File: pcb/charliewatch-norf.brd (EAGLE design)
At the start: 33 x 33 mm, 84 parts, among them K1 TS-1188E, U2 CC430F5137IRGZR, X1 CRYSTALS-NOGND-IQXC-25

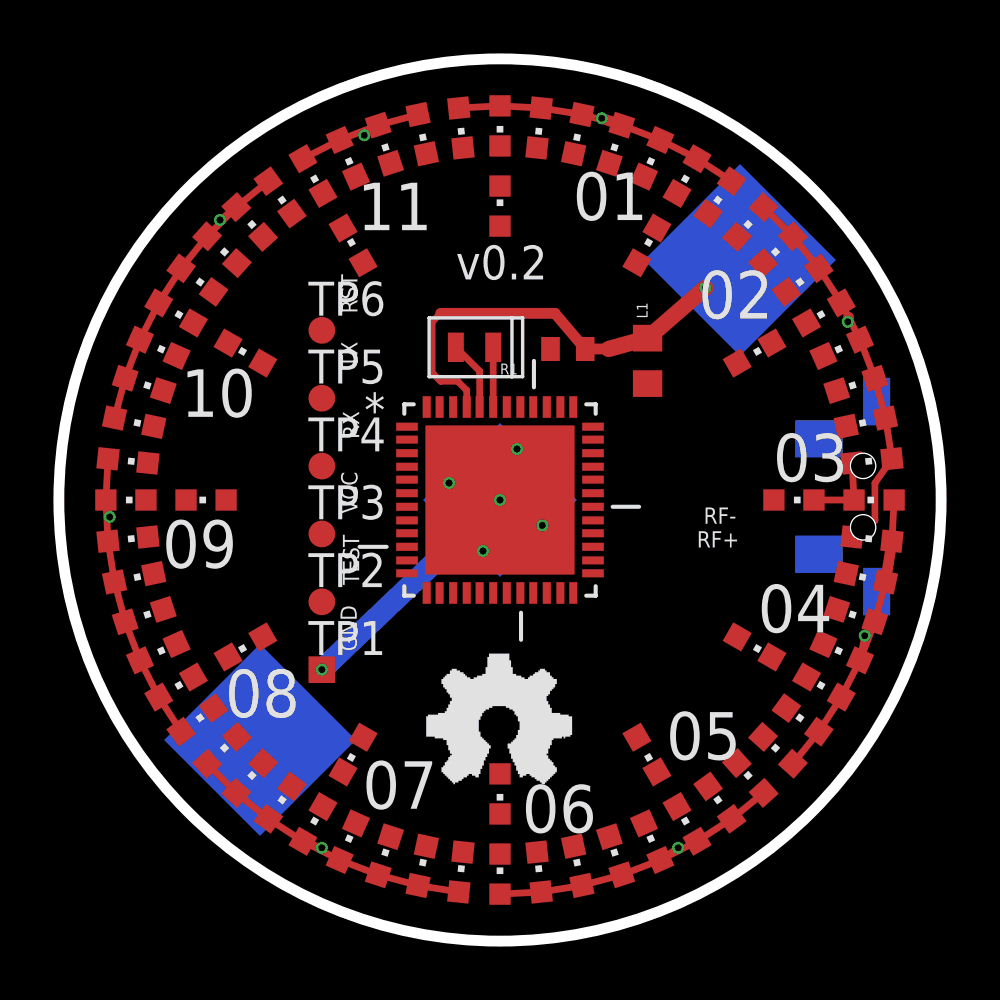
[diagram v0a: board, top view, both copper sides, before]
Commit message: slightly smaller, still routable version with no RF components
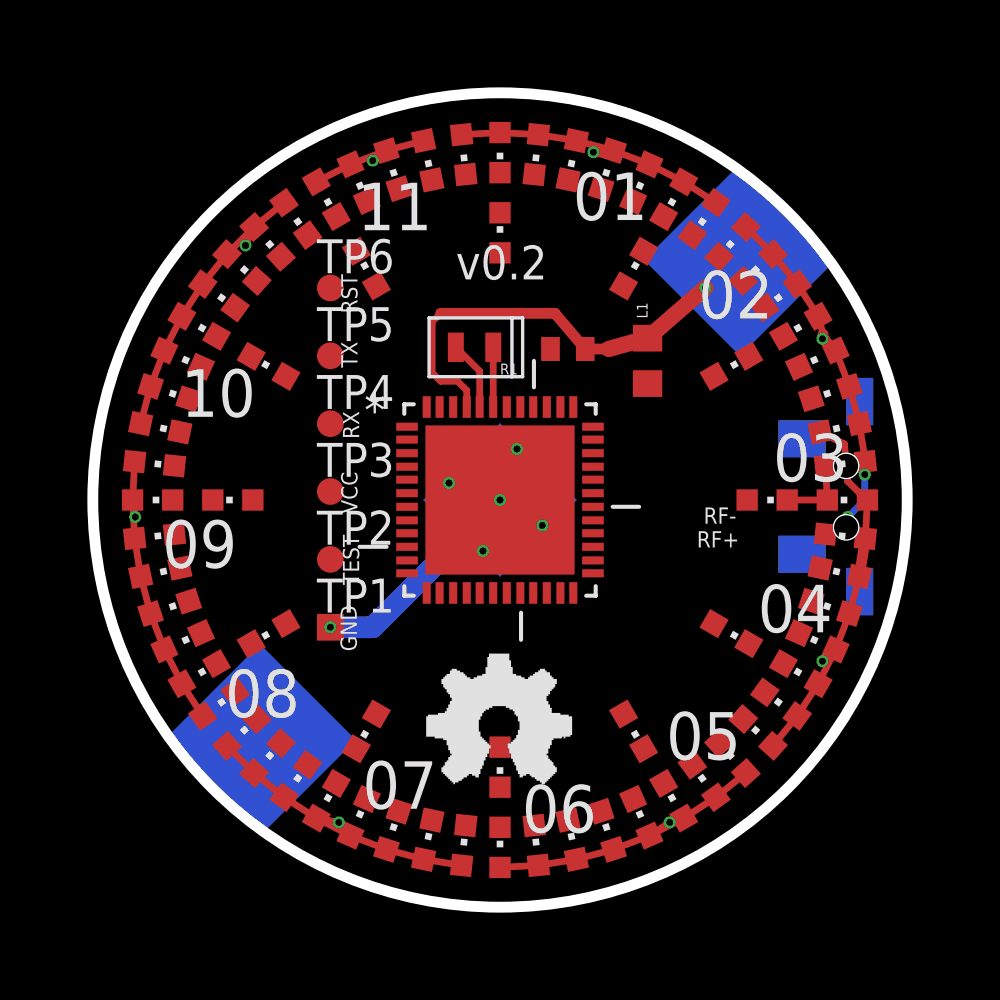
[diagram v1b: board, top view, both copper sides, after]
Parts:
- moved TP3 1.62 mm to (19.1, 25.7)
- moved TP1 1.62 mm to (19.1, 20.6)
- moved TP2 1.62 mm to (19.1, 23.2)
- moved TP4 1.62 mm to (19.1, 28.3)
- moved TP5 1.62 mm to (19.1, 30.8)
- moved TP6 1.62 mm to (19.1, 33.3)
- moved LED25 1.00 mm to (26.8, 12.5)
- moved LED32 1.00 mm to (24.0, 12.5)
- moved LED40 1.00 mm to (12.5, 26.8)
- moved LED42 1.00 mm to (12.5, 24.0)
- moved LED0 1.00 mm to (24.0, 38.3)
- moved LED17 1.00 mm to (38.3, 24.0)
- moved LED2 1.00 mm to (26.8, 38.3)
- moved LED8 1.00 mm to (38.3, 26.8)
- moved LED1 1.00 mm to (25.4, 38.4)
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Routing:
- net B2: track 11.7 -> 14.2 mm
- net GND: track 22.1 -> 21.2 mm
- net B1: track 14.5 -> 13.7 mm, vias 1 -> 3
- net B0: track 14.5 -> 13.7 mm
- net B5: track 11.5 -> 10.7 mm
- net B6: track 11.6 -> 10.8 mm
- net B3: track 11.6 -> 11.0 mm
- net B4: track 11.6 -> 10.9 mm
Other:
- board size 33 x 33 mm -> 30.5 x 30.5 mm
